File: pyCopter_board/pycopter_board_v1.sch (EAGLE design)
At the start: 36 parts, among them Q1 32.768kHz, U1 BNO055, U3 BMP180

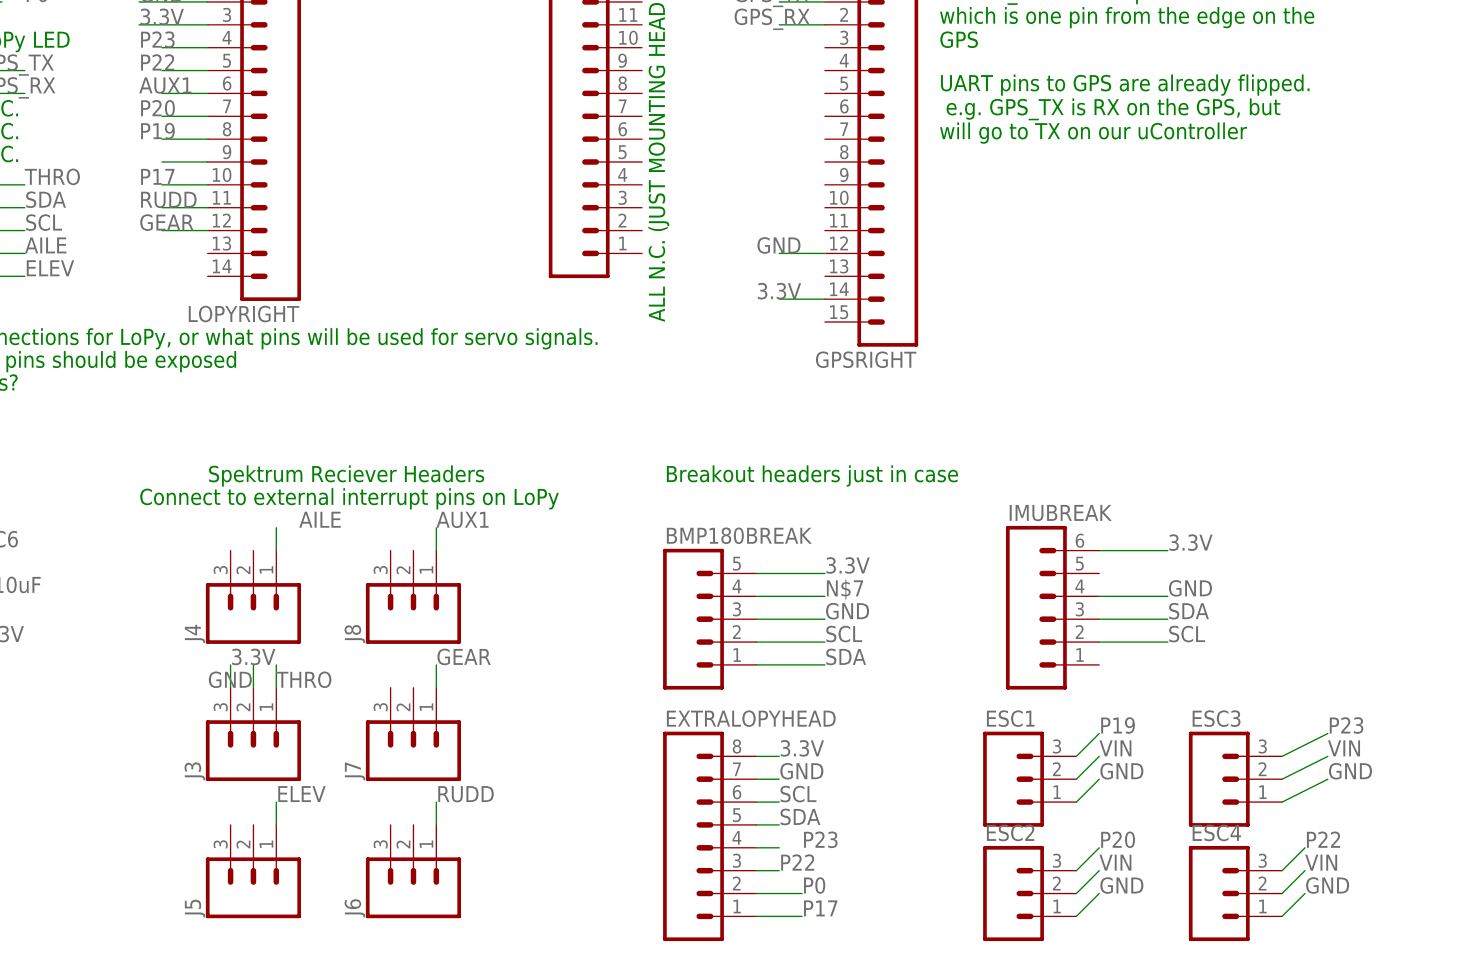
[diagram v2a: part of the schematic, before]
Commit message: board is all connected as is. Will try for another version in the morning which has more components on the bottom.
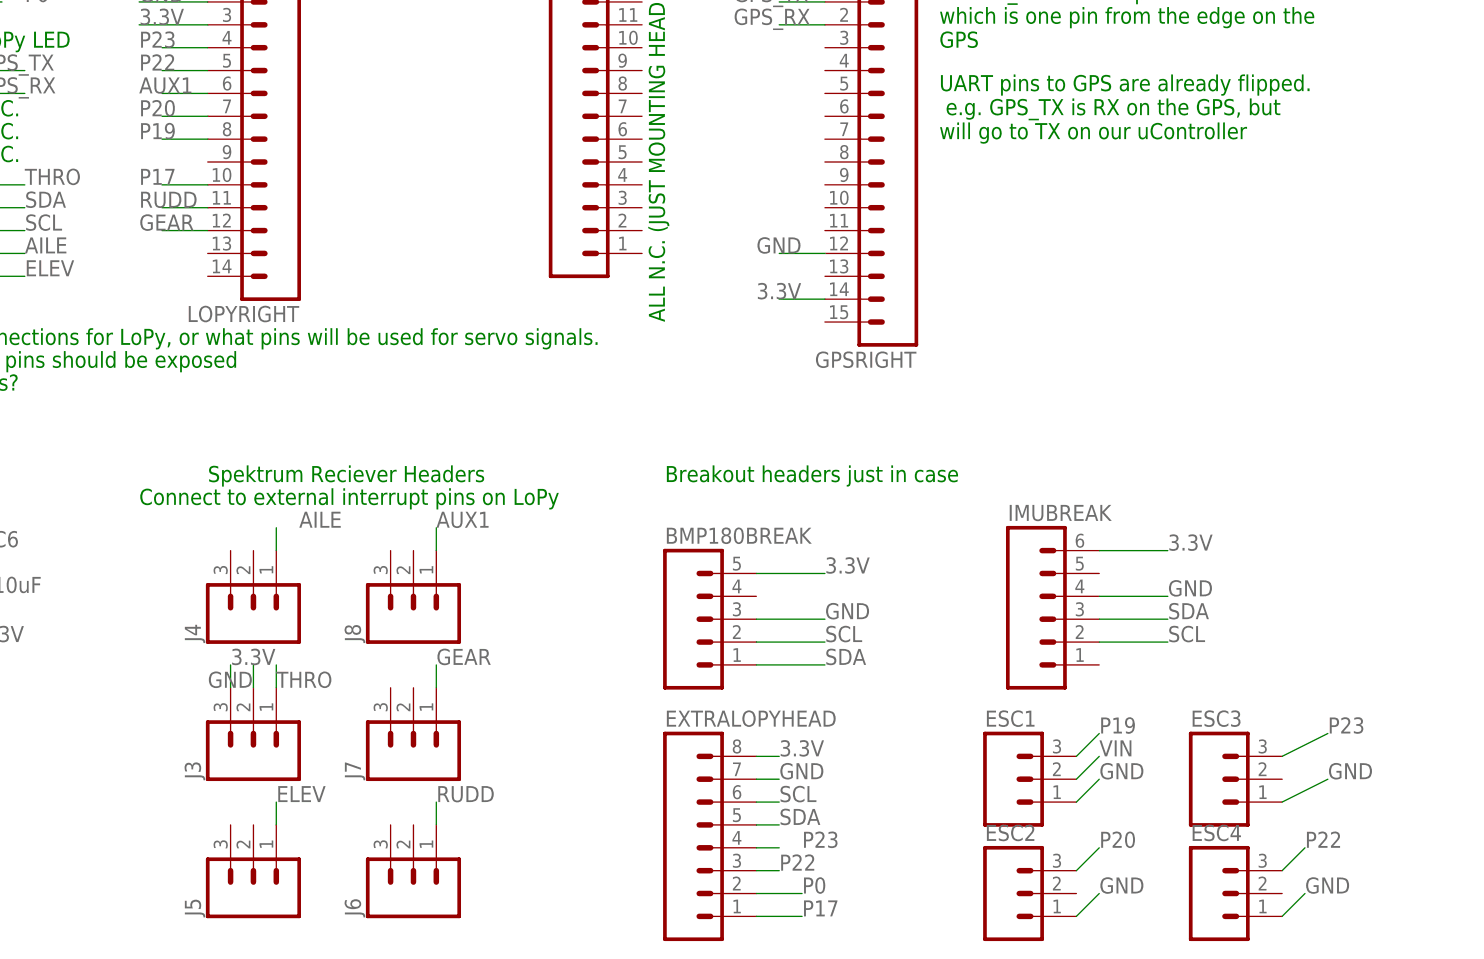
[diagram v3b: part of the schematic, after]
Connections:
- removed net N$7: BMP180BREAK.4
- removed net N$9: LOPYRIGHT.9
- net VIN: no longer ESC2.2, ESC3.2, ESC4.2
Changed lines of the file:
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@@
 <label x="185.42" y="-22.86" size="1.778" layer="95"/>
-</segment>
-<segment>
-<pinref part="ESC3" gate="J$1" pin="2"/>
-<wire x1="205.74" y1="-25.4" x2="210.82" y2="-22.86" width="0.1524" layer="91"/>
-<label x="210.82" y="-22.86" size="1.778" layer="95"/>
-</segment>
-<segment>
-<pinref part="ESC4" gate="J$1" pin="2"/>
-<wire x1="205.74" y1="-38.1" x2="208.28" y2="-35.56" width="0.1524" layer="91"/>
-<label x="208.28" y="-35.56" size="1.778" layer="95"/>
-</segment>
-<segment>
-<pinref part="ESC2" gate="J$1" pin="2"/>
-<wire x1="182.88" y1="-38.1" x2="185.42" y2="-35.56" width="0.1524" layer="91"/>
-<label x="185.42" y="-35.56" size="1.778" layer="95"/>
 </segment>
 </net>
@@
 </segment>
 </net>
-<net name="N$7" class="0">
-<segment>
-<pinref part="BMP180BREAK" gate="G$1" pin="4"/>
-<wire x1="147.32" y1="-5.08" x2="154.94" y2="-5.08" width="0.1524" layer="91"/>
-<label x="154.94" y="-5.08" size="1.778" layer="95"/>
-</segment>
-</net>
 <net name="THRO" class="0">
 <segment>
@@
 </segment>
 </net>
-<net name="N$9" class="0">
-<segment>
-<pinref part="LOPYRIGHT" gate="G$1" pin="9"/>
-<wire x1="86.36" y1="43.18" x2="81.28" y2="43.18" width="0.1524" layer="91"/>
-</segment>
-</net>
 <net name="P0" class="0">
 <segment>
@@
 </sheet>
 </sheets>
+<errors>
+</errors>
 </schematic>
 </drawing>

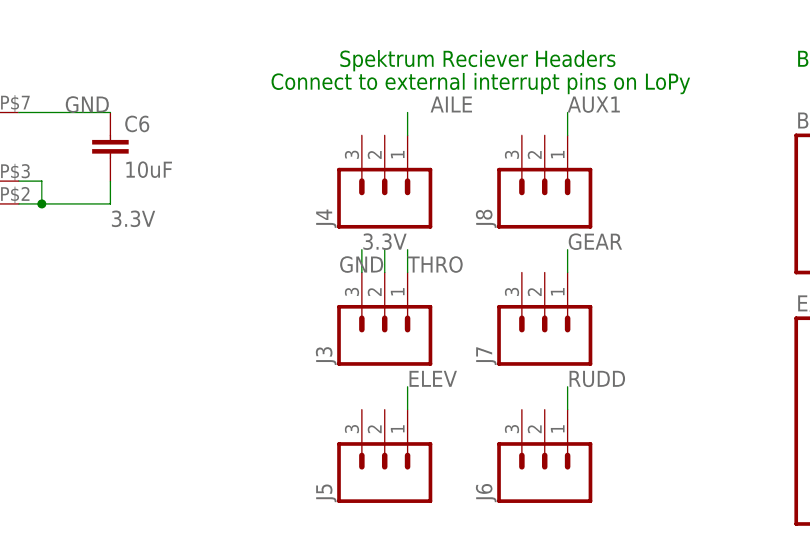
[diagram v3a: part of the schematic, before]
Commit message: at a good base point for autorouter. The power traces are all thicker, and routed the all the radio transmitter pins to the outside of the LoPy.
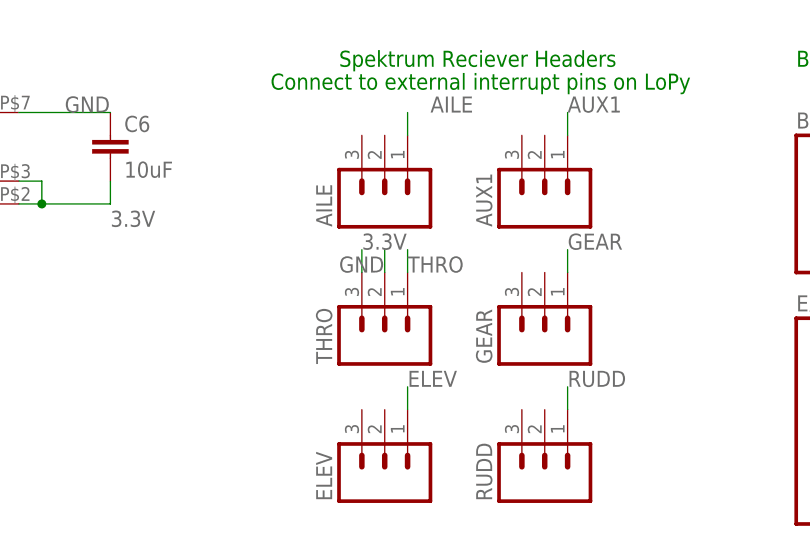
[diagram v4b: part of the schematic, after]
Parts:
- renumbered J3 to THRO, J4 to AILE, J5 to ELEV, J6 to RUDD, J7 to GEAR, J8 to AUX1
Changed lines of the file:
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@@
 <part name="GPSLEFT" library="SparkFun-Connectors" deviceset="M12" device="PTH"/>
 <part name="GPSRIGHT" library="SparkFun-Connectors" deviceset="M15" device=""/>
-<part name="J3" library="SparkFun-Connectors" deviceset="M03" device="PTH"/>
-<part name="J4" library="SparkFun-Connectors" deviceset="M03" device="PTH"/>
-<part name="J5" library="SparkFun-Connectors" deviceset="M03" device="PTH"/>
-<part name="J6" library="SparkFun-Connectors" deviceset="M03" device="PTH"/>
-<part name="J7" library="SparkFun-Connectors" deviceset="M03" device="PTH"/>
-<part name="J8" library="SparkFun-Connectors" deviceset="M03" device="PTH"/>
+<part name="THRO" library="SparkFun-Connectors" deviceset="M03" device="PTH"/>
+<part name="AILE" library="SparkFun-Connectors" deviceset="M03" device="PTH"/>
+<part name="ELEV" library="SparkFun-Connectors" deviceset="M03" device="PTH"/>
+<part name="RUDD" library="SparkFun-Connectors" deviceset="M03" device="PTH"/>
+<part name="GEAR" library="SparkFun-Connectors" deviceset="M03" device="PTH"/>
+<part name="AUX1" library="SparkFun-Connectors" deviceset="M03" device="PTH"/>
 <part name="IMUBREAK" library="SparkFun-Connectors" deviceset="M06" device="SILK_FEMALE_PTH"/>
 <part name="BMP180BREAK" library="SparkFun-Connectors" deviceset="M05" device="PTH"/>
@@
 <instance part="GPSLEFT" gate="G$1" x="124.46" y="48.26"/>
 <instance part="GPSRIGHT" gate="G$1" x="165.1" y="43.18" rot="R180"/>
-<instance part="J3" gate="J$1" x="91.44" y="-22.86" rot="R90"/>
-<instance part="J4" gate="J$1" x="91.44" y="-7.62" rot="R90"/>
-<instance part="J5" gate="J$1" x="91.44" y="-38.1" rot="R90"/>
-<instance part="J6" gate="J$1" x="109.22" y="-38.1" rot="R90"/>
-<instance part="J7" gate="J$1" x="109.22" y="-22.86" rot="R90"/>
-<instance part="J8" gate="J$1" x="109.22" y="-7.62" rot="R90"/>
+<instance part="THRO" gate="J$1" x="91.44" y="-22.86" rot="R90"/>
+<instance part="AILE" gate="J$1" x="91.44" y="-7.62" rot="R90"/>
+<instance part="ELEV" gate="J$1" x="91.44" y="-38.1" rot="R90"/>
+<instance part="RUDD" gate="J$1" x="109.22" y="-38.1" rot="R90"/>
+<instance part="GEAR" gate="J$1" x="109.22" y="-22.86" rot="R90"/>
+<instance part="AUX1" gate="J$1" x="109.22" y="-7.62" rot="R90"/>
 <instance part="IMUBREAK" gate="G$1" x="180.34" y="-7.62"/>
 <instance part="BMP180BREAK" gate="G$1" x="139.7" y="-7.62"/>
@@
 </segment>
 <segment>
-<pinref part="J3" gate="J$1" pin="3"/>
+<pinref part="THRO" gate="J$1" pin="3"/>
 <wire x1="88.9" y1="-15.24" x2="88.9" y2="-12.7" width="0.1524" layer="91"/>
 <label x="86.36" y="-15.24" size="1.778" layer="95"/>
@@
 </segment>
 <segment>
-<pinref part="J3" gate="J$1" pin="2"/>
+<pinref part="THRO" gate="J$1" pin="2"/>
 <wire x1="91.44" y1="-15.24" x2="91.44" y2="-12.7" width="0.1524" layer="91"/>
 <label x="88.9" y="-12.7" size="1.778" layer="95"/>
@@
 <net name="THRO" class="0">
 <segment>
-<pinref part="J3" gate="J$1" pin="1"/>
+<pinref part="THRO" gate="J$1" pin="1"/>
 <wire x1="93.98" y1="-15.24" x2="93.98" y2="-12.7" width="0.1524" layer="91"/>
 <label x="93.98" y="-15.24" size="1.778" layer="95"/>
@@
 <net name="ELEV" class="0">
 <segment>
-<pinref part="J5" gate="J$1" pin="1"/>
+<pinref part="ELEV" gate="J$1" pin="1"/>
 <wire x1="93.98" y1="-30.48" x2="93.98" y2="-27.94" width="0.1524" layer="91"/>
 <label x="93.98" y="-27.94" size="1.778" layer="95"/>
@@
 <net name="RUDD" class="0">
 <segment>
-<pinref part="J6" gate="J$1" pin="1"/>
+<pinref part="RUDD" gate="J$1" pin="1"/>
 <wire x1="111.76" y1="-30.48" x2="111.76" y2="-27.94" width="0.1524" layer="91"/>
 <label x="111.76" y="-27.94" size="1.778" layer="95"/>
@@
 <net name="GEAR" class="0">
 <segment>
-<pinref part="J7" gate="J$1" pin="1"/>
+<pinref part="GEAR" gate="J$1" pin="1"/>
 <wire x1="111.76" y1="-15.24" x2="111.76" y2="-12.7" width="0.1524" layer="91"/>
 <label x="111.76" y="-12.7" size="1.778" layer="95"/>
@@
 <net name="AUX1" class="0">
 <segment>
-<pinref part="J8" gate="J$1" pin="1"/>
+<pinref part="AUX1" gate="J$1" pin="1"/>
 <wire x1="111.76" y1="0" x2="111.76" y2="2.54" width="0.1524" layer="91"/>
 <label x="111.76" y="2.54" size="1.778" layer="95"/>
@@
 <net name="AILE" class="0">
 <segment>
-<pinref part="J4" gate="J$1" pin="1"/>
+<pinref part="AILE" gate="J$1" pin="1"/>
 <wire x1="93.98" y1="0" x2="93.98" y2="2.54" width="0.1524" layer="91"/>
 <label x="96.52" y="2.54" size="1.778" layer="95"/>
